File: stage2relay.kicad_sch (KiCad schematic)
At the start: 5 parts, among them SW2 SW_Push, U4 PY14-02

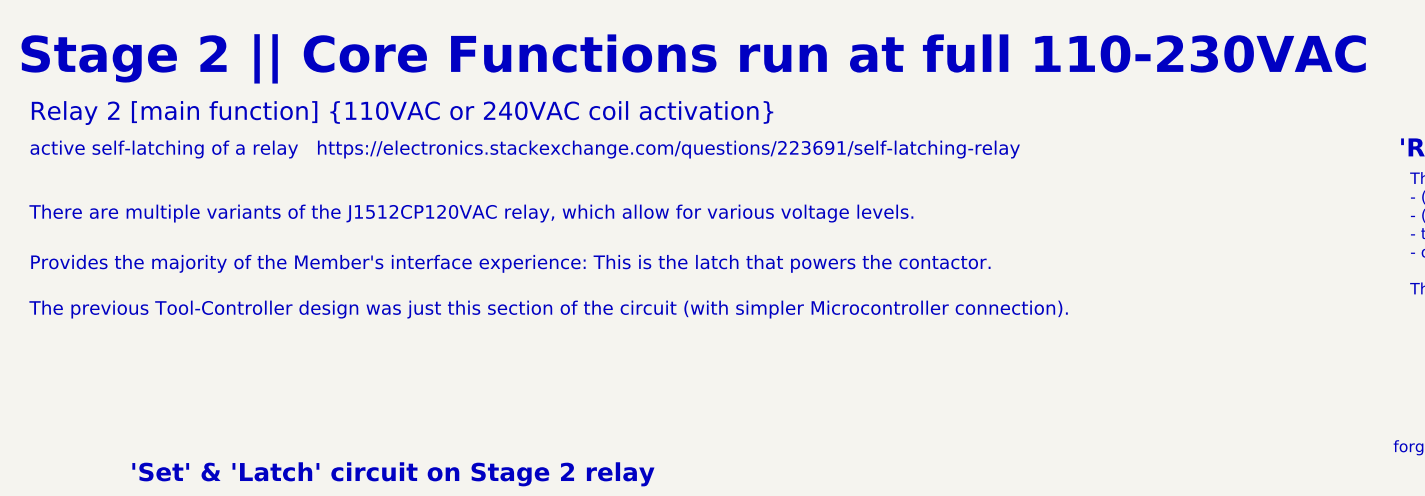
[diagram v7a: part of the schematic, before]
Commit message: local variant of PY14-02 footprint
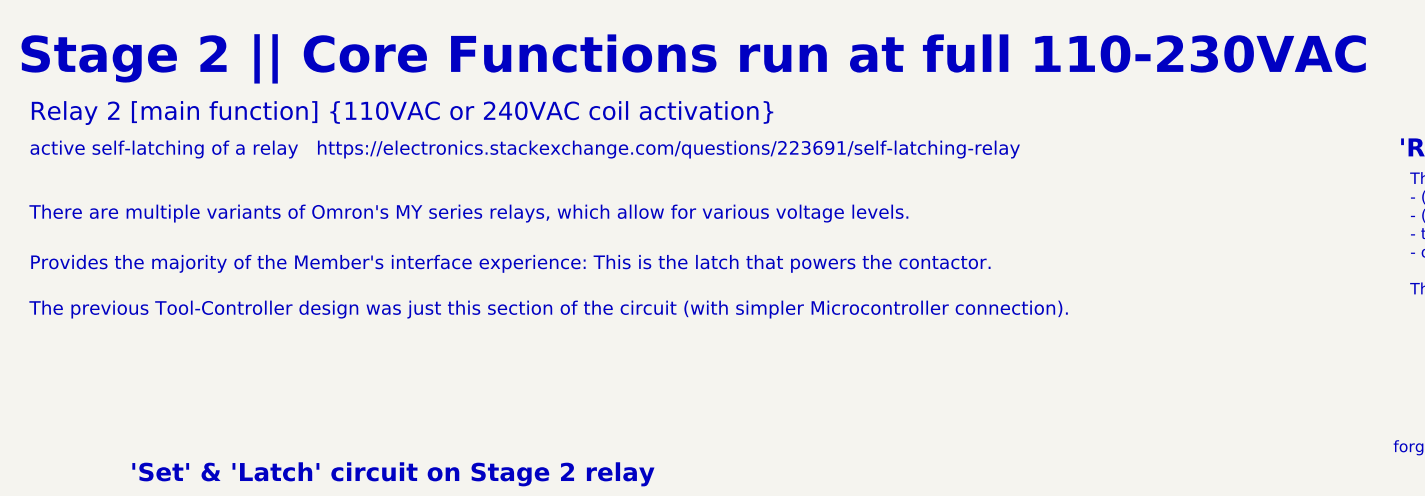
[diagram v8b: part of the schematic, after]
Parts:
- U4: footprint mk_relay_socket:RELAY-TH_PY14-02 -> Library:Relay_Socket_4PDT_Omron_PY14-02-local
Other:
- note added: "There are multiple variants of Omron's MY series relays, which allow for various voltage levels."
- note removed: "There are multiple variants of the J1512CP120VAC relay, which allow for various voltage levels."
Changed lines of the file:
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@@
 		)
 	)
-	(text "There are multiple variants of the J1512CP120VAC relay, which allow for various voltage levels."
+	(text "There are multiple variants of Omron's MY series relays, which allow for various voltage levels."
 		(exclude_from_sim no)
 		(at 21.59 37.592 0)
@@
 			)
 		)
-		(property "Footprint" "mk_relay_socket:RELAY-TH_PY14-02"
+		(property "Footprint" "Library:Relay_Socket_4PDT_Omron_PY14-02-local"
 			(at 66.802 151.638 0)
 			(effects
